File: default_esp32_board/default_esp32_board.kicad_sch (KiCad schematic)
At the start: 60 parts, among them IC1 TPS56339DDCR, IC2 TPS56339DDCR, J10 5V_T1, J3 Pwr, J4 Conn_01x15_Socket, J5 ZED_F9P_MOD, J6 Conn_01x15_Socket, J7 5V_T1, J8 3V3_T2, J9 3V3_T1

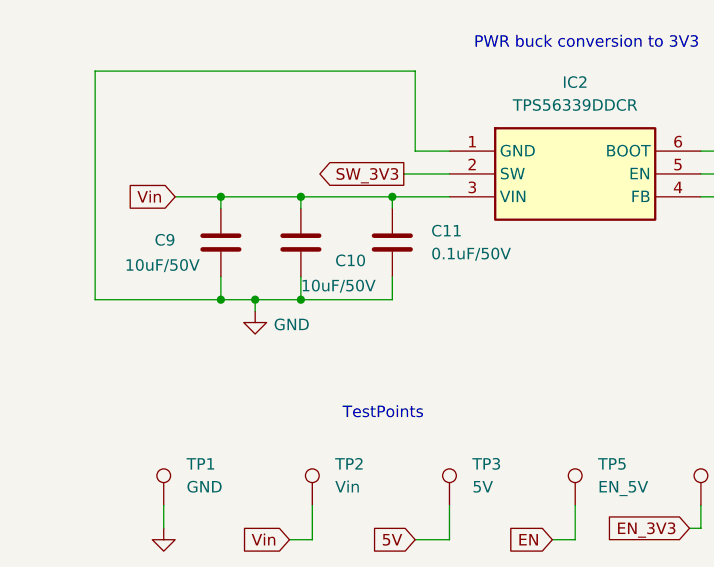
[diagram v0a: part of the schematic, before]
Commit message: Changed bad ESP32 30 pin footprint, changed bucks footprints to make it easier to solder in the new version
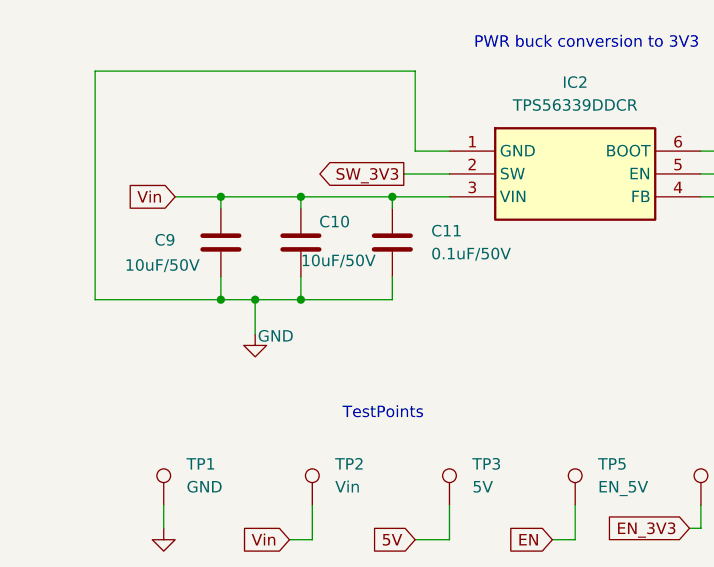
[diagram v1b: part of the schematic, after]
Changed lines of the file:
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@@
 	)
 	(junction
-		(at 33.02 165.1)
+		(at 114.3 104.14)
 		(diameter 0)
 		(color 0 0 0 0)
 	)
 	(junction
-		(at 114.3 104.14)
+		(at 33.02 165.1)
 		(diameter 0)
 		(color 0 0 0 0)
@@
 	(wire
 		(pts
-			(xy 33.02 165.1) (xy 29.21 165.1)
+			(xy 29.21 165.1) (xy 33.02 165.1)
 		)
 		(stroke
@@
 	(wire
 		(pts
+			(xy 33.02 165.1) (xy 38.1 165.1)
+		)
+		(stroke
+			(width 0)
+			(type default)
+		)
+	)
+	(wire
+		(pts
 			(xy 158.75 110.49) (xy 158.75 104.14)
 		)
@@
 	(wire
 		(pts
-			(xy 33.02 165.1) (xy 38.1 165.1)
-		)
-		(stroke
-			(width 0)
-			(type default)
-		)
-	)
-	(wire
-		(pts
 			(xy 165.1 49.53) (xy 168.91 49.53)
 		)
@@
 	(wire
 		(pts
-			(xy 33.02 165.1) (xy 33.02 166.37)
+			(xy 33.02 165.1) (xy 33.02 168.91)
 		)
 		(stroke
@@
 	(symbol
 		(lib_id "power:GND")
-		(at 33.02 166.37 0)
+		(at 33.02 168.91 0)
 		(unit 1)
 		(exclude_from_sim no)
@@
 		(dnp no)
 		(property "Reference" "#PWR017"
-			(at 33.02 172.72 0)
+			(at 33.02 175.26 0)
 			(effects
 				(font
@@
 		)
 		(property "Value" "GND"
-			(at 37.084 167.894 0)
+			(at 35.306 169.164 0)
 			(effects
 				(font
@@
 		)
 		(property "Footprint" ""
-			(at 33.02 166.37 0)
+			(at 33.02 168.91 0)
 			(effects
 				(font
@@
 		)
 		(property "Datasheet" ""
-			(at 33.02 166.37 0)
+			(at 33.02 168.91 0)
 			(effects
 				(font
@@
 		)
 		(property "Description" "Power symbol creates a global label with name \"GND\" , ground"
-			(at 33.02 166.37 0)
+			(at 33.02 168.91 0)
 			(effects
 				(font
@@
 		(dnp no)
 		(property "Reference" "C10"
-			(at 41.91 160.782 0)
+			(at 40.132 156.464 0)
 			(effects
 				(font
@@
 		)
 		(property "Value" "10uF/50V"
-			(at 38.1 163.576 0)
+			(at 38.1 160.782 0)
 			(effects
 				(font
